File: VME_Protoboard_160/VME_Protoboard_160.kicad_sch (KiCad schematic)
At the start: 55 parts, among them J1 Conn_02x08_Odd_Even, J2 Conn_02x08_Odd_Even, J3 Conn_02x12_Odd_Even, J4 Conn_02x07_Odd_Even, U1 74x16245, U2 74x16245, U3 74x16245, U4 74x1G19, U5 74x1G07, U6 74x1G07, U7 74x1G125, U8 74x1G125, U9 74x1G125, X1 DIN41612_03x32_ABC_VMEbus

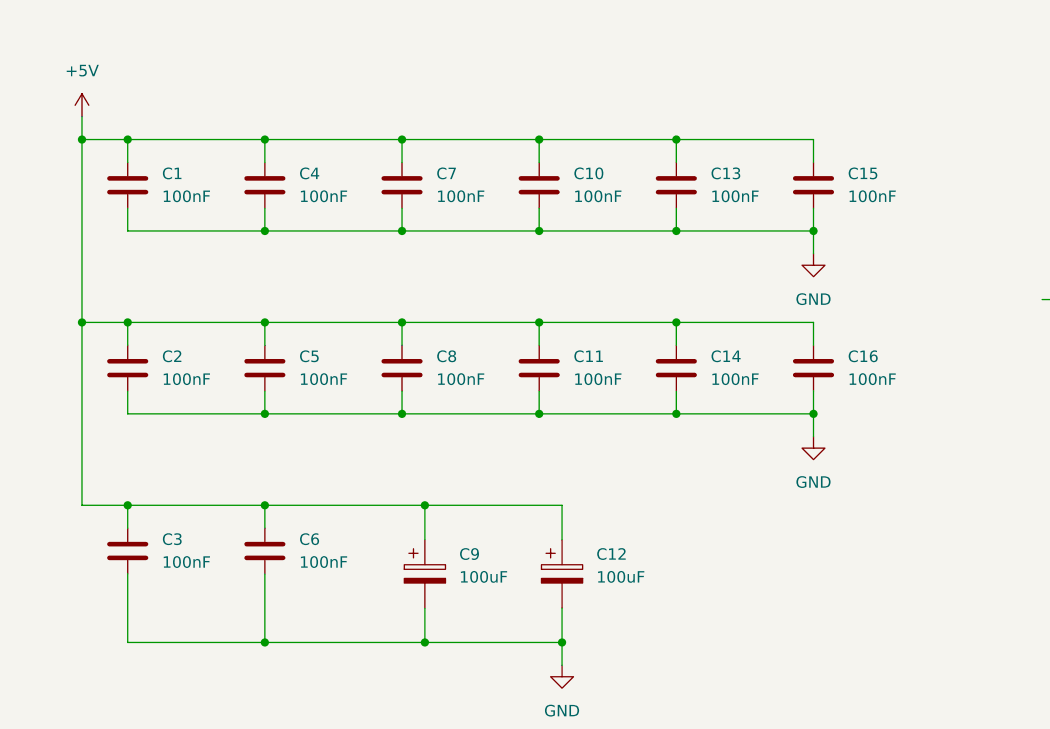
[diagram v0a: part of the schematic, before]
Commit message: Final touches, 160mm board ready for production
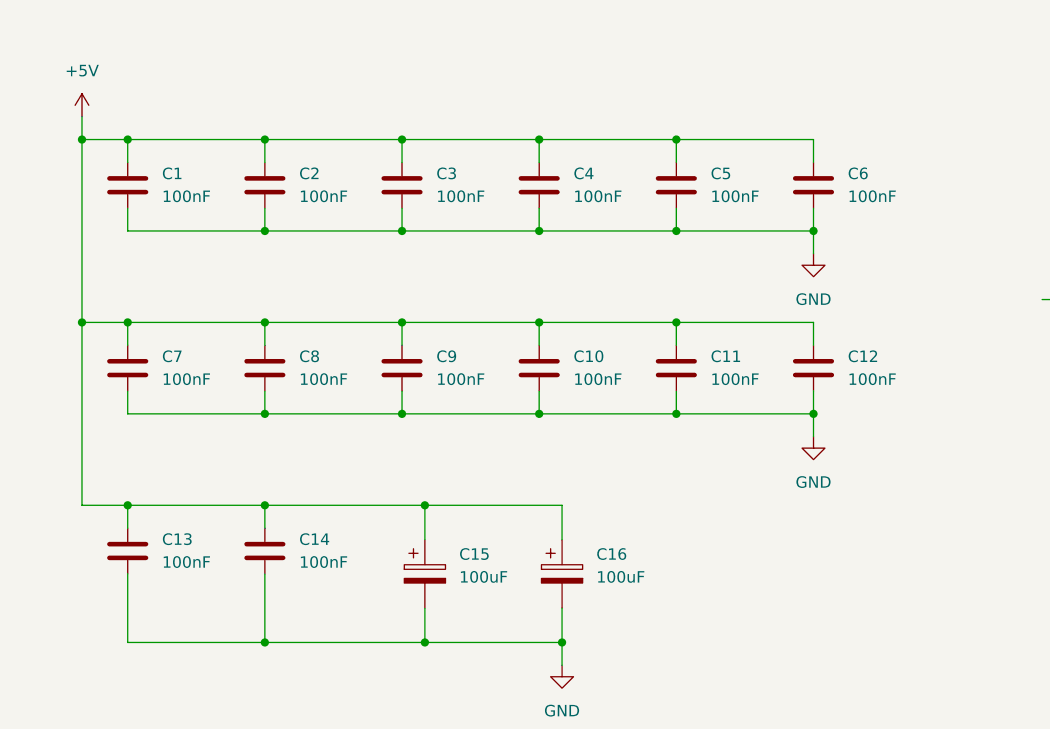
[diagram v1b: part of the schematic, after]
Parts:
- renumbered C11 to C10, C14 to C11, C16 to C12, C3 to C13, C6 to C14, C9 to C15, C12 to C16, C4 to C2, C7 to C3, C10 to C4, C13 to C5, C15 to C6, C2 to C7, C5 to C8, C8 to C9
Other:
- company: (none) -> (C) TOM STOREY
- title: (none) -> VMEbus PROTOTYPING BOARD, 160MM
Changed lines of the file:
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@@
 (kicad_sch (version 20211123) (generator eeschema)
   (paper "A3")
+  (title_block
+    (title "VMEbus PROTOTYPING BOARD, 160MM")
+    (date "2023-11-11")
+    (rev "1")
+    (company "(C) TOM STOREY")
+    (comment 1 "FREE FOR NON-COMMERCIAL USE")
+  )
   (junction (at 165.1 246.38) (diameter 0) (color 0 0 0 0)
   )
@@
   (symbol (lib_id "COMET_symbols:C") (at 226.06 220.98 0) (unit 1)
     (in_bom yes) (on_board yes) (fields_autoplaced)
-    (property "Reference" "C15" (id 0) (at 229.87 219.7099 0)
+    (property "Reference" "C6" (id 0) (at 229.87 219.7099 0)
       (effects (font (size 1.27 1.27)) (justify left))
     )
@@
   (symbol (lib_id "COMET_symbols:C") (at 195.58 241.3 0) (unit 1)
     (in_bom yes) (on_board yes) (fields_autoplaced)
-    (property "Reference" "C11" (id 0) (at 199.39 240.0299 0)
+    (property "Reference" "C10" (id 0) (at 199.39 240.0299 0)
       (effects (font (size 1.27 1.27)) (justify left))
     )
@@
   (symbol (lib_id "COMET_symbols:C") (at 180.34 241.3 0) (unit 1)
     (in_bom yes) (on_board yes) (fields_autoplaced)
-    (property "Reference" "C8" (id 0) (at 184.15 240.0299 0)
+    (property "Reference" "C9" (id 0) (at 184.15 240.0299 0)
       (effects (font (size 1.27 1.27)) (justify left))
     )
@@
   (symbol (lib_id "COMET_symbols:C") (at 165.1 241.3 0) (unit 1)
     (in_bom yes) (on_board yes) (fields_autoplaced)
-    (property "Reference" "C5" (id 0) (at 168.91 240.0299 0)
+    (property "Reference" "C8" (id 0) (at 168.91 240.0299 0)
       (effects (font (size 1.27 1.27)) (justify left))
     )
@@
   (symbol (lib_id "COMET_symbols:C") (at 149.86 241.3 0) (unit 1)
     (in_bom yes) (on_board yes) (fields_autoplaced)
-    (property "Reference" "C2" (id 0) (at 153.67 240.0299 0)
+    (property "Reference" "C7" (id 0) (at 153.67 240.0299 0)
       (effects (font (size 1.27 1.27)) (justify left))
     )
@@
   (symbol (lib_id "COMET_symbols:C") (at 226.06 241.3 0) (unit 1)
     (in_bom yes) (on_board yes) (fields_autoplaced)
-    (property "Reference" "C16" (id 0) (at 229.87 240.0299 0)
+    (property "Reference" "C12" (id 0) (at 229.87 240.0299 0)
       (effects (font (size 1.27 1.27)) (justify left))
     )
@@
   (symbol (lib_id "COMET_symbols:C") (at 165.1 261.62 0) (unit 1)
     (in_bom yes) (on_board yes) (fields_autoplaced)
-    (property "Reference" "C6" (id 0) (at 168.91 260.3499 0)
+    (property "Reference" "C14" (id 0) (at 168.91 260.3499 0)
       (effects (font (size 1.27 1.27)) (justify left))
     )
@@
   (symbol (lib_id "COMET_symbols:C") (at 180.34 220.98 0) (unit 1)
     (in_bom yes) (on_board yes) (fields_autoplaced)
-    (property "Reference" "C7" (id 0) (at 184.15 219.7099 0)
+    (property "Reference" "C3" (id 0) (at 184.15 219.7099 0)
       (effects (font (size 1.27 1.27)) (justify left))
     )
@@
   (symbol (lib_id "COMET_symbols:C") (at 210.82 241.3 0) (unit 1)
     (in_bom yes) (on_board yes) (fields_autoplaced)
-    (property "Reference" "C14" (id 0) (at 214.63 240.0299 0)
+    (property "Reference" "C11" (id 0) (at 214.63 240.0299 0)
       (effects (font (size 1.27 1.27)) (justify left))
     )
@@
   (symbol (lib_id "COMET_symbols:C") (at 165.1 220.98 0) (unit 1)
     (in_bom yes) (on_board yes) (fields_autoplaced)
-    (property "Reference" "C4" (id 0) (at 168.91 219.7099 0)
+    (property "Reference" "C2" (id 0) (at 168.91 219.7099 0)
       (effects (font (size 1.27 1.27)) (justify left))
     )
@@
   (symbol (lib_id "Device:C_Polarized") (at 182.88 264.16 0) (unit 1)
     (in_bom yes) (on_board yes) (fields_autoplaced)
-    (property "Reference" "C9" (id 0) (at 186.69 262.0009 0)
+    (property "Reference" "C15" (id 0) (at 186.69 262.0009 0)
       (effects (font (size 1.27 1.27)) (justify left))
     )
@@
   (symbol (lib_id "Device:C_Polarized") (at 198.12 264.16 0) (unit 1)
     (in_bom yes) (on_board yes) (fields_autoplaced)
-    (property "Reference" "C12" (id 0) (at 201.93 262.0009 0)
+    (property "Reference" "C16" (id 0) (at 201.93 262.0009 0)
       (effects (font (size 1.27 1.27)) (justify left))
     )
@@
   (symbol (lib_id "COMET_symbols:C") (at 210.82 220.98 0) (unit 1)
     (in_bom yes) (on_board yes) (fields_autoplaced)
-    (property "Reference" "C13" (id 0) (at 214.63 219.7099 0)
+    (property "Reference" "C5" (id 0) (at 214.63 219.7099 0)
       (effects (font (size 1.27 1.27)) (justify left))
     )
@@
   (symbol (lib_id "COMET_symbols:C") (at 195.58 220.98 0) (unit 1)
     (in_bom yes) (on_board yes) (fields_autoplaced)
-    (property "Reference" "C10" (id 0) (at 199.39 219.7099 0)
+    (property "Reference" "C4" (id 0) (at 199.39 219.7099 0)
       (effects (font (size 1.27 1.27)) (justify left))
     )
@@
   (symbol (lib_id "COMET_symbols:C") (at 149.86 261.62 0) (unit 1)
     (in_bom yes) (on_board yes) (fields_autoplaced)
-    (property "Reference" "C3" (id 0) (at 153.67 260.3499 0)
+    (property "Reference" "C13" (id 0) (at 153.67 260.3499 0)
       (effects (font (size 1.27 1.27)) (justify left))
     )
@@
       (reference "C1") (unit 1) (value "100nF") (footprint "COMET_footprints:C_SMD0805")
     )
-    (path "/37d2a6de-8e5a-4b85-9f09-1cdc8935b7aa"
+    (path "/9d9bc76c-7881-4834-b3ba-03078f5a37ab"
       (reference "C2") (unit 1) (value "100nF") (footprint "COMET_footprints:C_SMD0805")
     )
-    (path "/e15bb0f8-2adb-4d2a-be36-c865a4765e4d"
+    (path "/9a68dc55-c954-434c-a8f4-c99db220eb01"
       (reference "C3") (unit 1) (value "100nF") (footprint "COMET_footprints:C_SMD0805")
     )
-    (path "/9d9bc76c-7881-4834-b3ba-03078f5a37ab"
+    (path "/d9827e5b-3e37-47fb-ac9a-982862830164"
       (reference "C4") (unit 1) (value "100nF") (footprint "COMET_footprints:C_SMD0805")
     )
-    (path "/30244e0a-87fb-4037-a406-16a158cb1dcf"
+    (path "/bb592069-747f-48b6-bb4c-5f4ab5809af7"
       (reference "C5") (unit 1) (value "100nF") (footprint "COMET_footprints:C_SMD0805")
     )
-    (path "/905a8a9c-b71a-4b8a-9643-500b4f4a73d4"
+    (path "/14212bdf-5cde-4d77-859e-1011eb603440"
       (reference "C6") (unit 1) (value "100nF") (footprint "COMET_footprints:C_SMD0805")
     )
-    (path "/9a68dc55-c954-434c-a8f4-c99db220eb01"
+    (path "/37d2a6de-8e5a-4b85-9f09-1cdc8935b7aa"
       (reference "C7") (unit 1) (value "100nF") (footprint "COMET_footprints:C_SMD0805")
     )
-    (path "/24b1bfba-a3d5-48d3-8335-569b7ae55422"
+    (path "/30244e0a-87fb-4037-a406-16a158cb1dcf"
       (reference "C8") (unit 1) (value "100nF") (footprint "COMET_footprints:C_SMD0805")
     )
-    (path "/a82f2fbd-c73e-47a9-9ed6-d8c22f62be5f"
-      (reference "C9") (unit 1) (value "100uF") (footprint "COMET_footprints:C_SMD_4.3MMx7.3MM")
+    (path "/24b1bfba-a3d5-48d3-8335-569b7ae55422"
+      (reference "C9") (unit 1) (value "100nF") (footprint "COMET_footprints:C_SMD0805")
     )
-    (path "/d9827e5b-3e37-47fb-ac9a-982862830164"
+    (path "/20dffc27-a2f8-40ca-8067-dc0ce46e1b30"
       (reference "C10") (unit 1) (value "100nF") (footprint "COMET_footprints:C_SMD0805")
     )
-    (path "/20dffc27-a2f8-40ca-8067-dc0ce46e1b30"
+    (path "/9b08e108-524b-4573-82a2-4f529931ad96"
       (reference "C11") (unit 1) (value "100nF") (footprint "COMET_footprints:C_SMD0805")
     )
-    (path "/a99c29e4-24d8-42a5-9c39-c0b4d8d58458"
-      (reference "C12") (unit 1) (value "100uF") (footprint "COMET_footprints:C_SMD_4.3MMx7.3MM")
+    (path "/6257b12b-44d7-46c4-b528-ce1423702b2e"
+      (reference "C12") (unit 1) (value "100nF") (footprint "COMET_footprints:C_SMD0805")
     )
-    (path "/bb592069-747f-48b6-bb4c-5f4ab5809af7"
+    (path "/e15bb0f8-2adb-4d2a-be36-c865a4765e4d"
       (reference "C13") (unit 1) (value "100nF") (footprint "COMET_footprints:C_SMD0805")
     )
-    (path "/9b08e108-524b-4573-82a2-4f529931ad96"
+    (path "/905a8a9c-b71a-4b8a-9643-500b4f4a73d4"
       (reference "C14") (unit 1) (value "100nF") (footprint "COMET_footprints:C_SMD0805")
     )
-    (path "/14212bdf-5cde-4d77-859e-1011eb603440"
-      (reference "C15") (unit 1) (value "100nF") (footprint "COMET_footprints:C_SMD0805")
+    (path "/a82f2fbd-c73e-47a9-9ed6-d8c22f62be5f"
+      (reference "C15") (unit 1) (value "100uF") (footprint "COMET_footprints:C_SMD_4.3MMx7.3MM")
     )
-    (path "/6257b12b-44d7-46c4-b528-ce1423702b2e"
-      (reference "C16") (unit 1) (value "100nF") (footprint "COMET_footprints:C_SMD0805")
+    (path "/a99c29e4-24d8-42a5-9c39-c0b4d8d58458"
+      (reference "C16") (unit 1) (value "100uF") (footprint "COMET_footprints:C_SMD_4.3MMx7.3MM")
     )
     (path "/d3ffd695-d981-4e2a-af11-93614a7812fe"

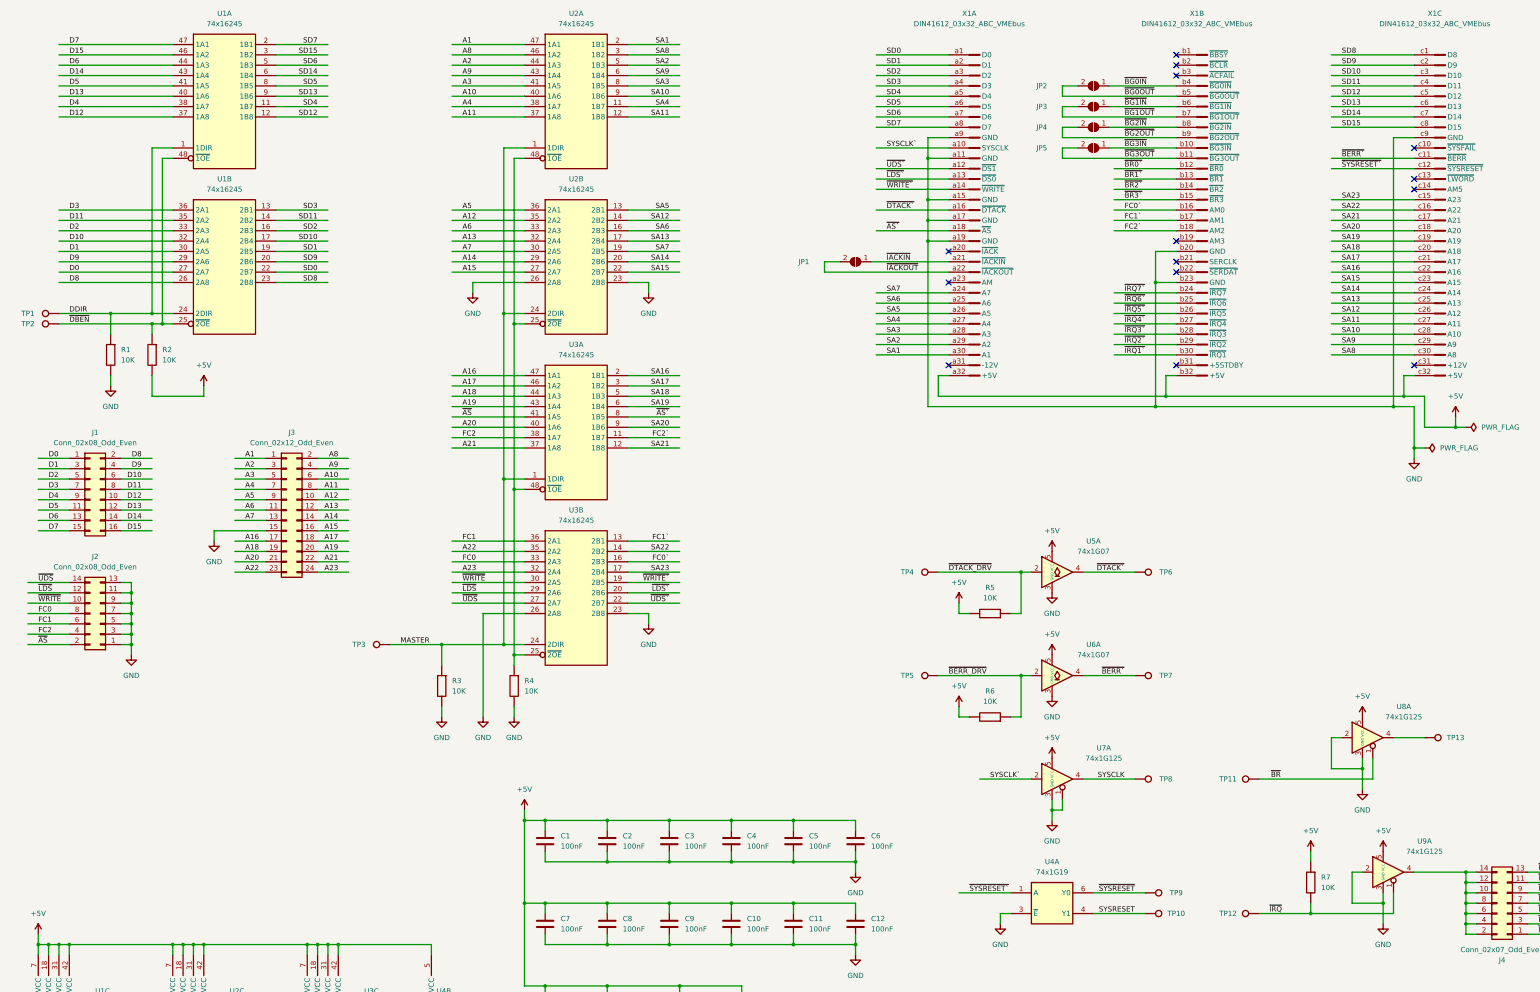
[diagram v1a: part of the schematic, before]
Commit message: Add extra test point for independent output control of each half of the data bus
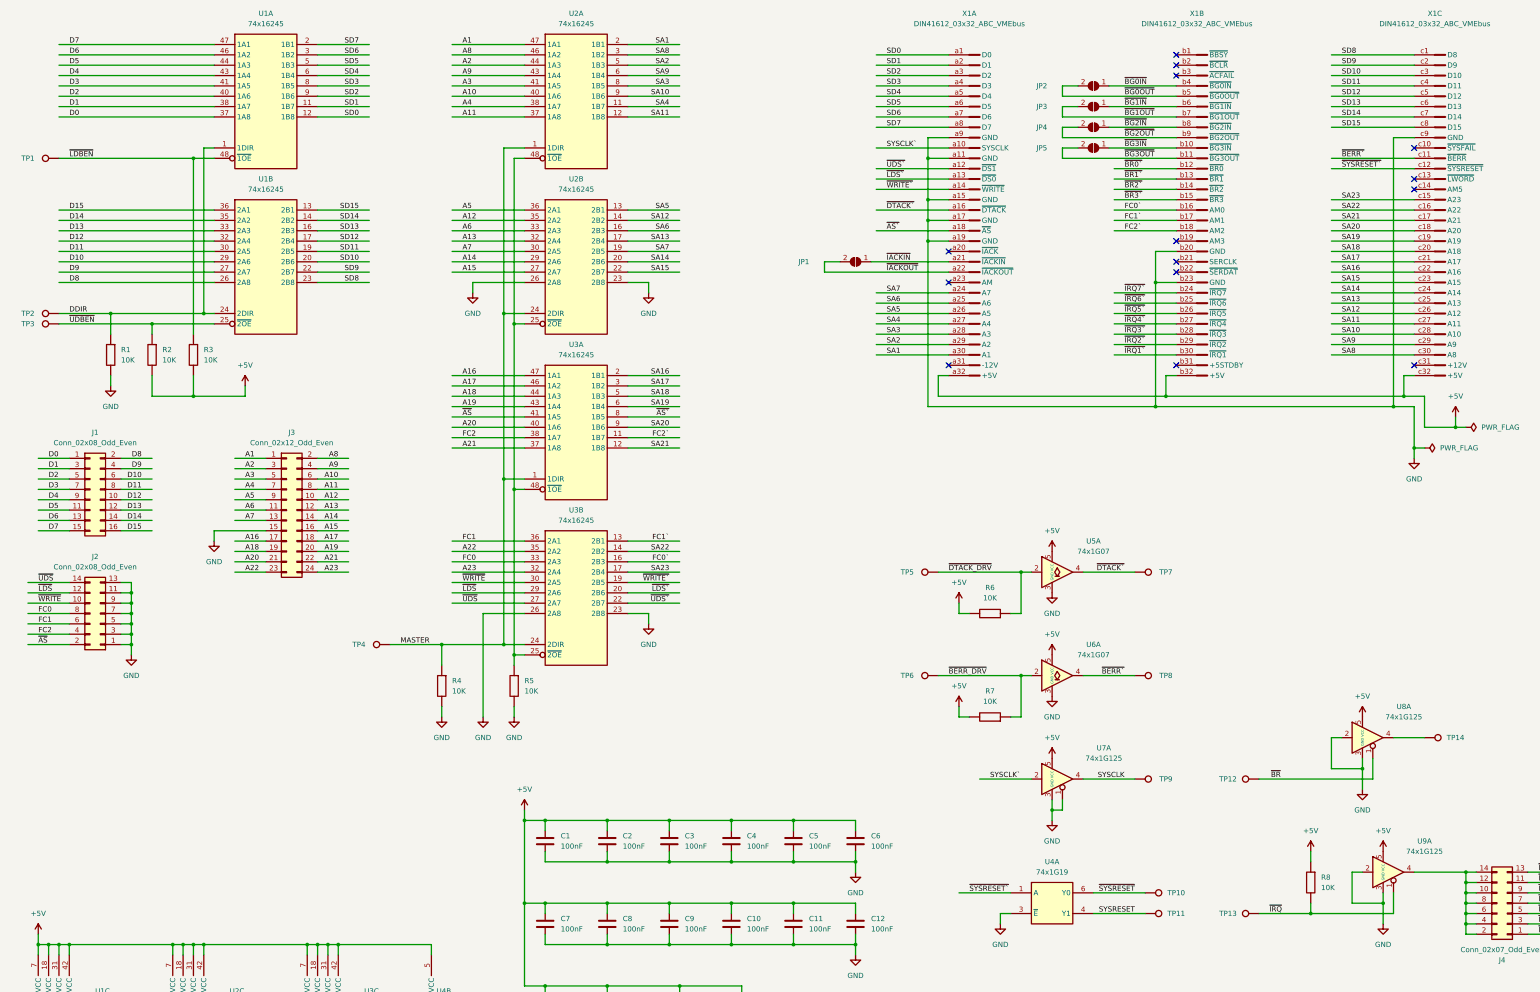
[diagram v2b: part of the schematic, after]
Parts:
- added R2: 10K, COMET_footprints:R_SMD0805, symbol COMET_symbols:R
- added TP1: TestPoint, TestPoint:TestPoint_Loop_D1.80mm_Drill1.0mm_Beaded, symbol Connector:TestPoint
- renumbered R2 to R3, R3 to R4, R4 to R5, R5 to R6, R6 to R7, R7 to R8, TP9 to TP10, TP10 to TP11, TP11 to TP12, TP12 to TP13, TP13 to TP14, TP1 to TP2, TP2 to TP3, TP3 to TP4, TP4 to TP5, TP5 to TP6, TP6 to TP7, TP7 to TP8, TP8 to TP9
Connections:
- net +5V: now also R2.1
- net D0: now also U1.37 (1A8); no longer U1.27 (2A7)
- net D1: now also U1.38 (1A7); no longer U1.30 (2A5)
- net D10: now also U1.29 (2A6); no longer U1.32 (2A4)
- net D11: now also U1.30 (2A5); no longer U1.35 (2A2)
- net D12: now also U1.32 (2A4); no longer U1.37 (1A8)
- net D13: now also U1.33 (2A3); no longer U1.40 (1A6)
- net D14: now also U1.35 (2A2); no longer U1.43 (1A4)
- net D15: now also U1.36 (2A1); no longer U1.46 (1A2)
- net D2: now also U1.40 (1A6); no longer U1.33 (2A3)
- net D3: now also U1.41 (1A5); no longer U1.36 (2A1)
- net D4: now also U1.43 (1A4); no longer U1.38 (1A7)
- net D5: now also U1.44 (1A3); no longer U1.41 (1A5)
- net D6: now also U1.46 (1A2); no longer U1.44 (1A3)
- net D9: now also U1.27 (2A7); no longer U1.29 (2A6)
- net SD0: now also U1.12 (1B8); no longer U1.22 (2B7)
- net SD1: now also U1.11 (1B7); no longer U1.19 (2B5)
- net SD10: now also U1.20 (2B6); no longer U1.17 (2B4)
- net SD11: now also U1.19 (2B5); no longer U1.14 (2B2)
- net SD12: now also U1.17 (2B4); no longer U1.12 (1B8)
- net SD13: now also U1.16 (2B3); no longer U1.9 (1B6)
- net SD14: now also U1.14 (2B2); no longer U1.6 (1B4)
- net SD15: now also U1.13 (2B1); no longer U1.3 (1B2)
- net SD2: now also U1.9 (1B6); no longer U1.16 (2B3)
- net SD3: now also U1.8 (1B5); no longer U1.13 (2B1)
- net SD4: now also U1.6 (1B4); no longer U1.11 (1B7)
- net SD5: now also U1.5 (1B3); no longer U1.8 (1B5)
- net SD6: now also U1.3 (1B2); no longer U1.5 (1B3)
- net SD9: now also U1.22 (2B7); no longer U1.20 (2B6)
- net ~{DBEN} renamed ~{LDBEN}
- net ~{LDBEN}: now also TP1.1; no longer TP3.1, U1.25 (~{2OE})
- new net ~{UDBEN}: R2.2, TP3.1, U1.25 (~{2OE})
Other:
- moved on the sheet: R3, U1A, U1B
